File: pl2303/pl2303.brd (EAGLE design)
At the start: 35.6 x 35.6 mm, 3 parts, among them SW1 SW_TACT_2P-3X6

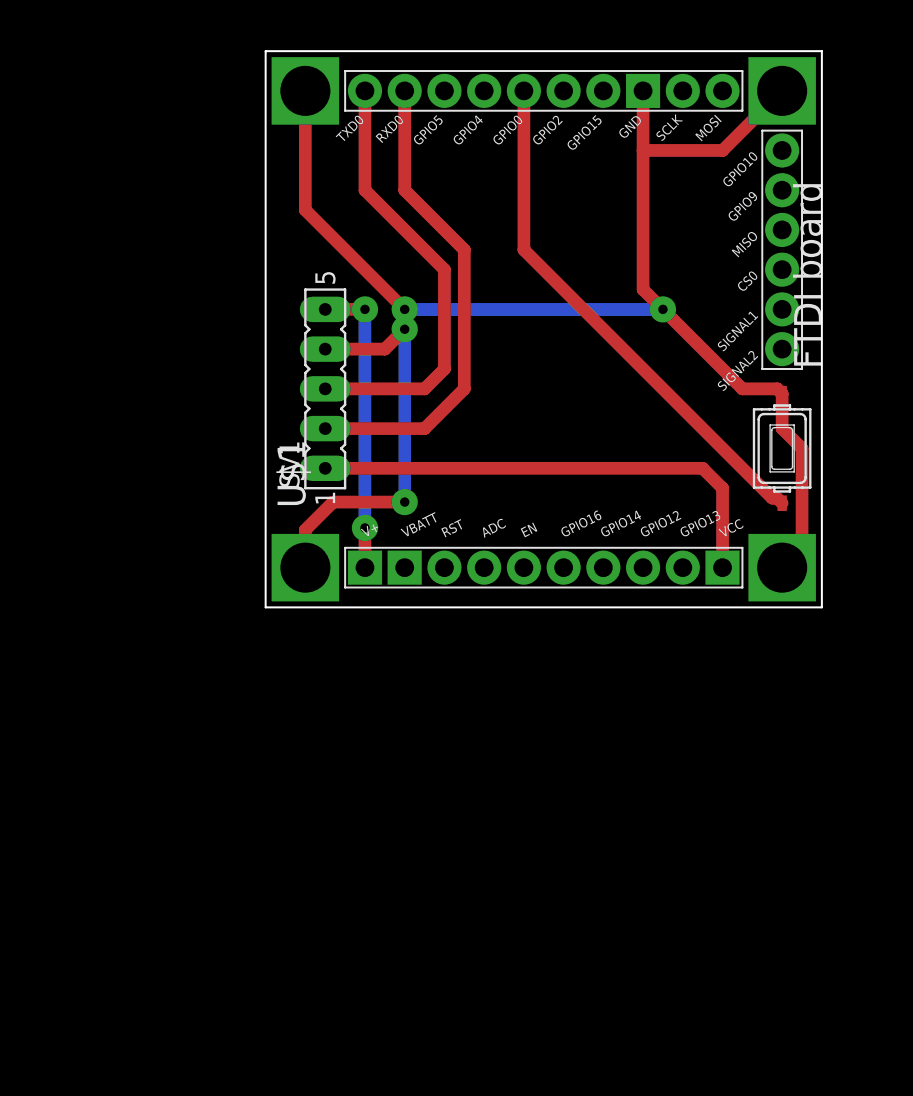
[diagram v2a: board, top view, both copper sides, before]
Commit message: New board schema applied to ftdi module
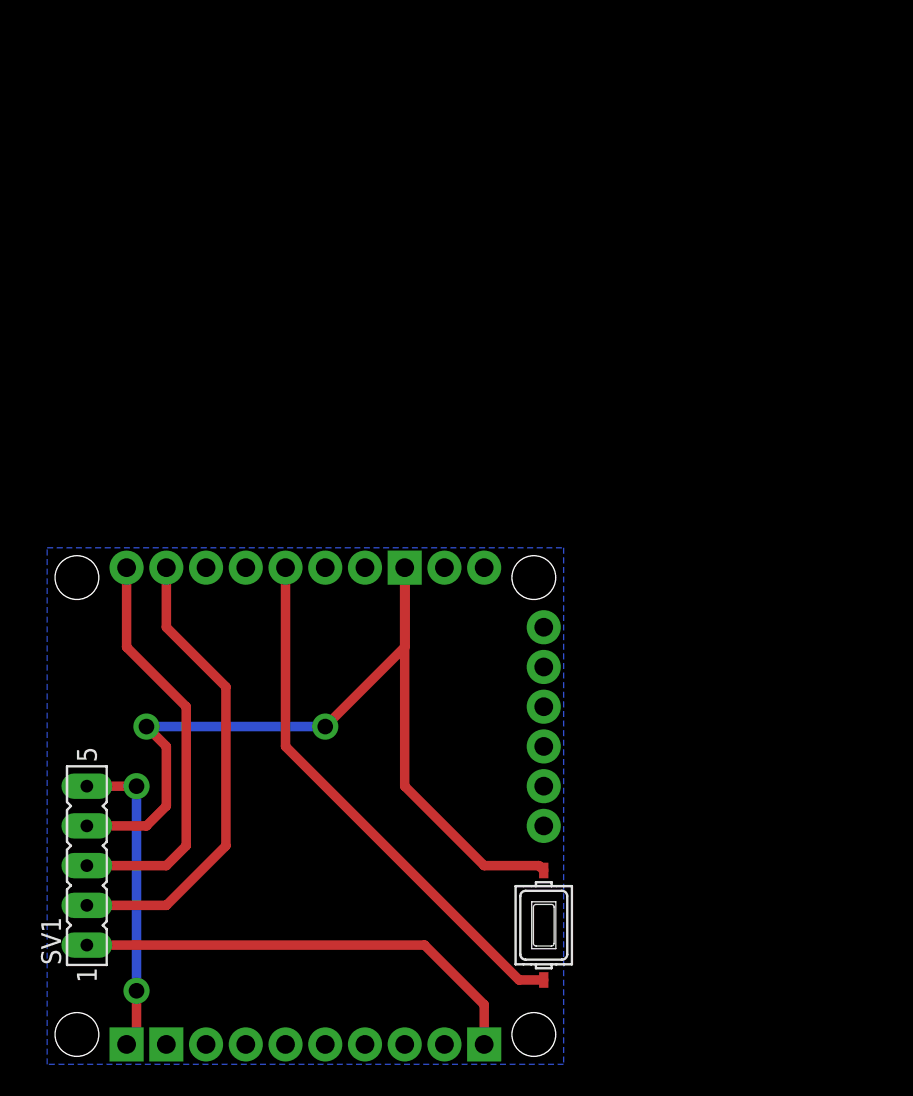
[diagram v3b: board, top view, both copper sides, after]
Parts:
- removed U$1: ESP-BOARD, ESPstack:ESP-BOARD
- added FTDI: ESP-BOARD, ESPstack:ESP-BOARD
- moved SV1 34.1 mm to (3.81, 14.0)
- moved SW1 34.1 mm to (33.0, 10.2)
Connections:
- net +3V3: now also FTDI.VCC; no longer U$1.VCC
- net +5V: now also FTDI.V+; no longer U$1.V+
- net GND: now also FTDI.GND; no longer U$1.GND@1, U$1.GND@2, U$1.GND@3, U$1.GND@4, U$1.GND@5
- net GPIO0: now also FTDI.GPIO0; no longer U$1.GPIO0
- net RXD0: now also FTDI.RXD0; no longer U$1.RXD0
- net TXD0: now also FTDI.TXD0; no longer U$1.TXD0
- net VBATT: now also FTDI.VBATT; no longer U$1.VBATT
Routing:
- net GND: track 107.5 -> 60.0 mm, vias 4 -> 2
- net TXD0: track 28.0 -> 26.2 mm
- net +3V3: track 31.0 -> 29.5 mm
- net +5V: track 19.0 -> 19.9 mm
- net GPIO0: track 33.4 -> 34.1 mm
- net RXD0: track 30.6 -> 29.8 mm
- added copper zone on layer 16, net GND
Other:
- board outline removed
- board text removed: "FTDI board"
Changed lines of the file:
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@@
 <setting verticaltext="up"/>
 </settings>
-<grid distance="0.05" unitdist="inch" unit="inch" style="lines" multiple="1" display="no" altdistance="0.005" altunitdist="inch" altunit="inch"/>
+<grid distance="0.05" unitdist="inch" unit="inch" style="lines" multiple="1" display="yes" altdistance="0.005" altunitdist="inch" altunit="inch"/>
 <layers>
 <layer number="1" name="Top" color="4" fill="1" visible="yes" active="yes"/>
@@
 <board>
 <plain>
-<text x="50.8" y="45.72" size="1.778" layer="25" rot="R90">FTDI board</text>
 </plain>
 <attributes>
@@
 </autorouter>
 <elements>
-<element name="SV1" library="con-lsta" package="FE05-1" value="" x="19.05" y="44.45" rot="R90">
-<attribute name="MF" value="" x="19.05" y="44.45" size="1.778" layer="27" rot="R90" display="off"/>
-<attribute name="OC_NEWARK" value="unknown" x="19.05" y="44.45" size="1.778" layer="27" rot="R90" display="off"/>
-<attribute name="OC_FARNELL" value="unknown" x="19.05" y="44.45" size="1.778" layer="27" rot="R90" display="off"/>
-<attribute name="MPN" value="" x="19.05" y="44.45" size="1.778" layer="27" rot="R90" display="off"/>
+<element name="SV1" library="con-lsta" package="FE05-1" value="" x="3.81" y="13.97" rot="R90">
+<attribute name="MF" value="" x="3.81" y="13.97" size="1.778" layer="27" rot="R90" display="off"/>
+<attribute name="OC_NEWARK" value="unknown" x="3.81" y="13.97" size="1.778" layer="27" rot="R90" display="off"/>
+<attribute name="OC_FARNELL" value="unknown" x="3.81" y="13.97" size="1.778" layer="27" rot="R90" display="off"/>
+<attribute name="MPN" value="" x="3.81" y="13.97" size="1.778" layer="27" rot="R90" display="off"/>
 </element>
-<element name="SW1" library="dp_devices" package="SW_TACT_3X6" value="SW_TACT_2P-3X6" x="48.26" y="40.64" rot="R270"/>
-<element name="U$1" library="ESPstack" package="ESP-BOARD" value="ESP-BOARD" x="39.37" y="49.53"/>
+<element name="SW1" library="dp_devices" package="SW_TACT_3X6" value="SW_TACT_2P-3X6" x="33.02" y="10.16" rot="R270"/>
+<element name="FTDI" library="ESPstack" package="ESP-BOARD" value="ESP-BOARD" x="24.13" y="19.05"/>
 </elements>
 <signals>
@@
 <contactref element="SW1" pad="1"/>
 <contactref element="SV1" pad="4"/>
-<contactref element="U$1" pad="GND@5"/>
-<contactref element="U$1" pad="GND@1"/>
-<contactref element="U$1" pad="GND@2"/>
-<contactref element="U$1" pad="GND@3"/>
-<contactref element="U$1" pad="GND@4"/>
-<wire x1="39.37" y1="63.5" x2="39.37" y2="59.69" width="0.8128" layer="1"/>
-<wire x1="39.37" y1="59.69" x2="39.37" y2="50.8" width="0.8128" layer="1"/>
-<wire x1="39.37" y1="50.8" x2="40.64" y2="49.53" width="0.8128" layer="1"/>
-<wire x1="45.72" y1="44.45" x2="47.95" y2="44.45" width="0.8128" layer="1"/>
-<wire x1="47.95" y1="44.45" x2="48.26" y2="44.14" width="0.8128" layer="1"/>
-<wire x1="48.26" y1="63.5" x2="44.45" y2="59.69" width="0.8128" layer="1"/>
-<wire x1="44.45" y1="59.69" x2="39.37" y2="59.69" width="0.8128" layer="1"/>
-<wire x1="48.26" y1="44.14" x2="48.26" y2="41.91" width="0.8128" layer="1"/>
-<wire x1="48.26" y1="41.91" x2="49.53" y2="40.64" width="0.8128" layer="1"/>
-<wire x1="49.53" y1="40.64" x2="49.53" y2="34.29" width="0.8128" layer="1"/>
-<wire x1="49.53" y1="34.29" x2="48.26" y2="33.02" width="0.8128" layer="1"/>
-<wire x1="17.78" y1="63.5" x2="17.78" y2="55.88" width="0.8128" layer="1"/>
-<wire x1="17.78" y1="55.88" x2="24.13" y2="49.53" width="0.8128" layer="1"/>
-<wire x1="17.78" y1="33.02" x2="17.78" y2="35.433" width="0.8128" layer="1"/>
-<wire x1="17.78" y1="35.433" x2="19.558" y2="37.211" width="0.8128" layer="1"/>
-<wire x1="19.05" y1="46.99" x2="22.86" y2="46.99" width="0.8128" layer="1"/>
-<wire x1="22.86" y1="46.99" x2="24.13" y2="48.26" width="0.8128" layer="1"/>
-<via x="24.13" y="49.53" extent="1-16" drill="0.6" diameter="1.6764" shape="octagon"/>
-<wire x1="24.13" y1="49.53" x2="40.64" y2="49.53" width="0.8128" layer="16"/>
-<via x="40.64" y="49.53" extent="1-16" drill="0.6" diameter="1.6764" shape="octagon"/>
-<wire x1="40.64" y1="49.53" x2="45.72" y2="44.45" width="0.8128" layer="1"/>
-<wire x1="19.558" y1="37.211" x2="24.13" y2="37.211" width="0.8128" layer="1"/>
-<via x="24.13" y="37.211" extent="1-16" drill="0.6" diameter="1.6764" shape="octagon"/>
-<wire x1="24.13" y1="37.211" x2="24.13" y2="48.26" width="0.8128" layer="16"/>
-<via x="24.13" y="48.26" extent="1-16" drill="0.6" diameter="1.6764" shape="octagon"/>
-<wire x1="24.13" y1="48.26" x2="24.13" y2="49.53" width="0.8128" layer="1"/>
+<contactref element="FTDI" pad="GND"/>
+<wire x1="3.81" y1="16.51" x2="7.62" y2="16.51" width="0.6096" layer="1"/>
+<wire x1="7.62" y1="16.51" x2="8.89" y2="17.78" width="0.6096" layer="1"/>
+<wire x1="8.89" y1="17.78" x2="8.89" y2="21.59" width="0.6096" layer="1"/>
+<wire x1="8.89" y1="21.59" x2="7.62" y2="22.86" width="0.6096" layer="1"/>
+<via x="7.62" y="22.86" extent="1-16" drill="1" diameter="1.6764"/>
+<wire x1="7.62" y1="22.86" x2="19.05" y2="22.86" width="0.6096" layer="16"/>
+<via x="19.05" y="22.86" extent="1-16" drill="1" diameter="1.6764"/>
+<wire x1="19.05" y1="22.86" x2="24.13" y2="27.94" width="0.6096" layer="1"/>
+<wire x1="24.13" y1="27.94" x2="24.13" y2="33.02" width="0.6096" layer="1"/>
+<wire x1="24.13" y1="33.02" x2="24.13" y2="19.05" width="0.6096" layer="1"/>
+<wire x1="24.13" y1="19.05" x2="29.21" y2="13.97" width="0.6096" layer="1"/>
+<wire x1="29.21" y1="13.97" x2="32.71" y2="13.97" width="0.6096" layer="1"/>
+<wire x1="32.71" y1="13.97" x2="33.02" y2="13.66" width="0.6096" layer="1"/>
+<polygon width="0.6096" layer="16" isolate="0.8128">
+<vertex x="1.27" y="34.29"/>
+<vertex x="34.29" y="34.29"/>
+<vertex x="34.29" y="1.27"/>
+<vertex x="1.27" y="1.27"/>
+</polygon>
 </signal>
 <signal name="+5V">
 <contactref element="SV1" pad="5"/>
-<contactref element="U$1" pad="V+"/>
-<wire x1="19.05" y1="49.53" x2="21.59" y2="49.53" width="0.8128" layer="1"/>
-<via x="21.59" y="49.53" extent="1-16" drill="0.6" diameter="1.6764"/>
-<wire x1="21.59" y1="49.53" x2="21.59" y2="35.56" width="0.8128" layer="16"/>
-<via x="21.59" y="35.56" extent="1-16" drill="0.6" diameter="1.6764" shape="square"/>
-<wire x1="21.59" y1="35.56" x2="21.59" y2="33.02" width="0.8128" layer="1"/>
+<contactref element="FTDI" pad="V+"/>
+<wire x1="3.81" y1="19.05" x2="6.985" y2="19.05" width="0.6096" layer="1"/>
+<via x="6.985" y="19.05" extent="1-16" drill="1" diameter="1.6764"/>
+<wire x1="6.985" y1="19.05" x2="6.985" y2="5.969" width="0.6096" layer="16"/>
+<via x="6.985" y="5.969" extent="1-16" drill="1" diameter="1.6764"/>
+<wire x1="6.985" y1="5.969" x2="6.985" y2="3.175" width="0.6096" layer="1"/>
+<wire x1="6.985" y1="3.175" x2="6.35" y2="2.54" width="0.6096" layer="1"/>
 </signal>
 <signal name="+3V3">
 <contactref element="SV1" pad="1"/>
-<contactref element="U$1" pad="VCC"/>
-<wire x1="19.05" y1="39.37" x2="43.18" y2="39.37" width="0.8128" layer="1"/>
-<wire x1="43.18" y1="39.37" x2="44.45" y2="38.1" width="0.8128" layer="1"/>
-<wire x1="44.45" y1="38.1" x2="44.45" y2="33.02" width="0.8128" layer="1"/>
+<contactref element="FTDI" pad="VCC"/>
+<wire x1="3.81" y1="8.89" x2="25.4" y2="8.89" width="0.6096" layer="1"/>
+<wire x1="25.4" y1="8.89" x2="29.21" y2="5.08" width="0.6096" layer="1"/>
+<wire x1="29.21" y1="5.08" x2="29.21" y2="2.54" width="0.6096" layer="1"/>
 </signal>
 <signal name="TXD0">
 <contactref element="SV1" pad="3"/>
-<contactref element="U$1" pad="TXD0"/>
-<wire x1="19.05" y1="44.45" x2="25.4" y2="44.45" width="0.8128" layer="1"/>
-<wire x1="25.4" y1="44.45" x2="26.67" y2="45.72" width="0.8128" layer="1"/>
-<wire x1="26.67" y1="45.72" x2="26.67" y2="52.07" width="0.8128" layer="1"/>
-<wire x1="26.67" y1="52.07" x2="21.59" y2="57.15" width="0.8128" layer="1"/>
-<wire x1="21.59" y1="57.15" x2="21.59" y2="63.5" width="0.8128" layer="1"/>
+<contactref element="FTDI" pad="TXD0"/>
+<wire x1="3.81" y1="13.97" x2="8.89" y2="13.97" width="0.6096" layer="1"/>
+<wire x1="8.89" y1="13.97" x2="10.16" y2="15.24" width="0.6096" layer="1"/>
+<wire x1="10.16" y1="15.24" x2="10.16" y2="24.13" width="0.6096" layer="1"/>
+<wire x1="10.16" y1="24.13" x2="6.35" y2="27.94" width="0.6096" layer="1"/>
+<wire x1="6.35" y1="27.94" x2="6.35" y2="33.02" width="0.6096" layer="1"/>
 </signal>
 <signal name="RXD0">
 <contactref element="SV1" pad="2"/>
-<contactref element="U$1" pad="RXD0"/>
-<wire x1="24.13" y1="63.5" x2="24.13" y2="57.15" width="0.8128" layer="1"/>
-<wire x1="24.13" y1="57.15" x2="27.94" y2="53.34" width="0.8128" layer="1"/>
-<wire x1="27.94" y1="53.34" x2="27.94" y2="44.45" width="0.8128" layer="1"/>
-<wire x1="27.94" y1="44.45" x2="25.4" y2="41.91" width="0.8128" layer="1"/>
-<wire x1="25.4" y1="41.91" x2="19.05" y2="41.91" width="0.8128" layer="1"/>
+<contactref element="FTDI" pad="RXD0"/>
+<wire x1="3.81" y1="11.43" x2="8.89" y2="11.43" width="0.6096" layer="1"/>
+<wire x1="8.89" y1="11.43" x2="12.7" y2="15.24" width="0.6096" layer="1"/>
+<wire x1="12.7" y1="15.24" x2="12.7" y2="25.4" width="0.6096" layer="1"/>
+<wire x1="12.7" y1="25.4" x2="8.89" y2="29.21" width="0.6096" layer="1"/>
+<wire x1="8.89" y1="29.21" x2="8.89" y2="33.02" width="0.6096" layer="1"/>
 </signal>
 <signal name="N$1">
@@
 <signal name="GPIO0">
 <contactref element="SW1" pad="2"/>
-<contactref element="U$1" pad="GPIO0"/>
-<wire x1="31.75" y1="63.5" x2="31.75" y2="53.34" width="0.8128" layer="1"/>
-<wire x1="31.75" y1="53.34" x2="47.625" y2="37.465" width="0.8128" layer="1"/>
-<wire x1="47.625" y1="37.465" x2="47.935" y2="37.465" width="0.8128" layer="1"/>
-<wire x1="47.935" y1="37.465" x2="48.26" y2="37.14" width="0.8128" layer="1"/>
+<contactref element="FTDI" pad="GPIO0"/>
+<wire x1="33.02" y1="6.66" x2="31.44" y2="6.66" width="0.6096" layer="1"/>
+<wire x1="31.44" y1="6.66" x2="16.51" y2="21.59" width="0.6096" layer="1"/>
+<wire x1="16.51" y1="21.59" x2="16.51" y2="33.02" width="0.6096" layer="1"/>
 </signal>
 <signal name="VBATT">
-<contactref element="U$1" pad="VBATT"/>
+<contactref element="FTDI" pad="VBATT"/>
 </signal>
 </signals>
